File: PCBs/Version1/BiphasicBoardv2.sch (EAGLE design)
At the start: 15 parts

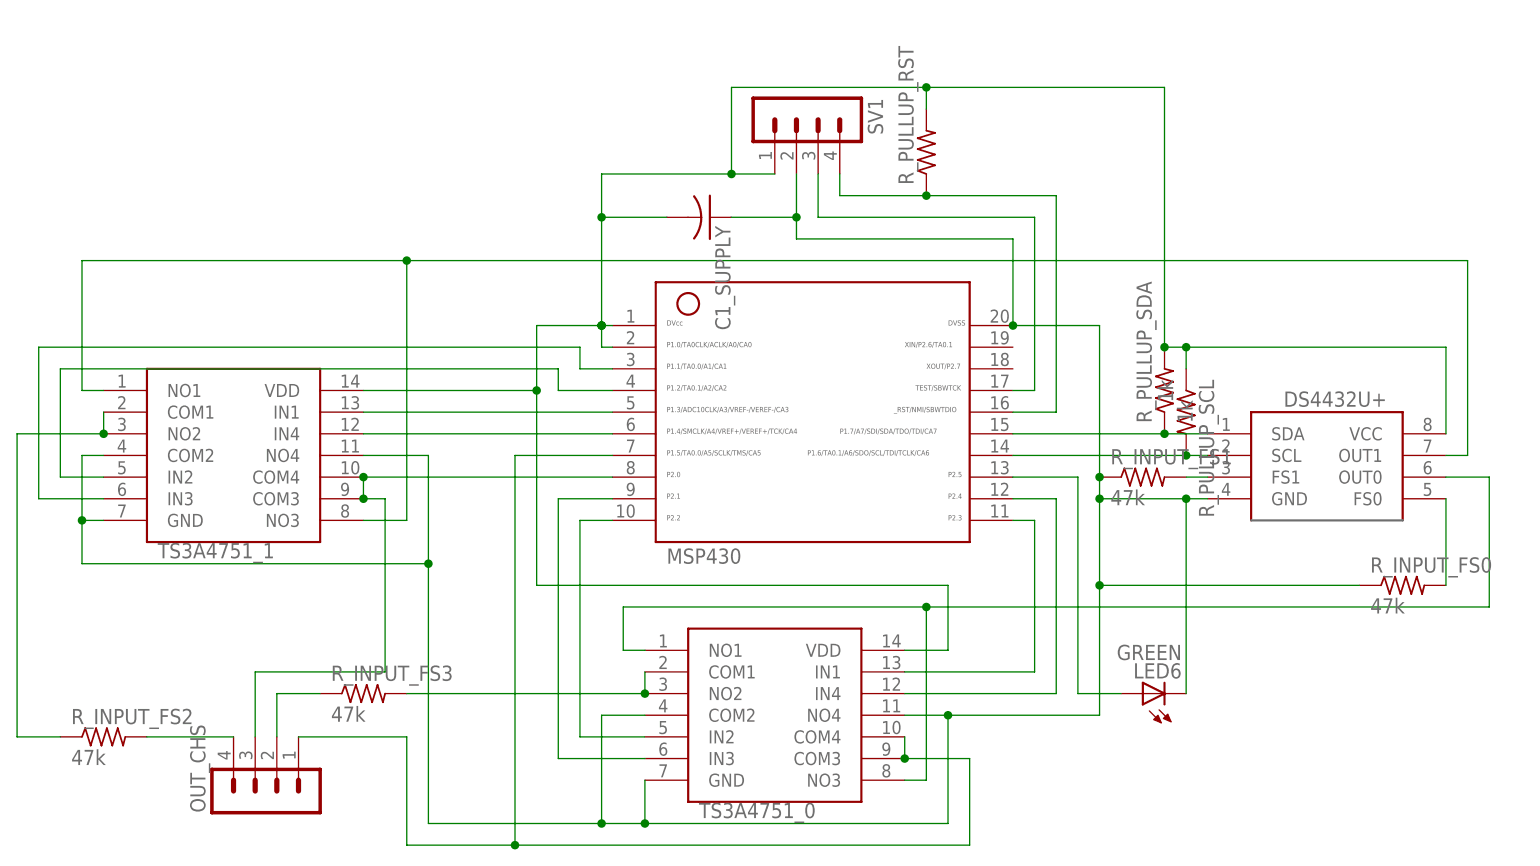
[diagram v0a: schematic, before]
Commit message: Version 1.1 Changes 1) Added a voltage divider to measure power supply level 2) Removed impedence measurement in one of the biphasic current output channels
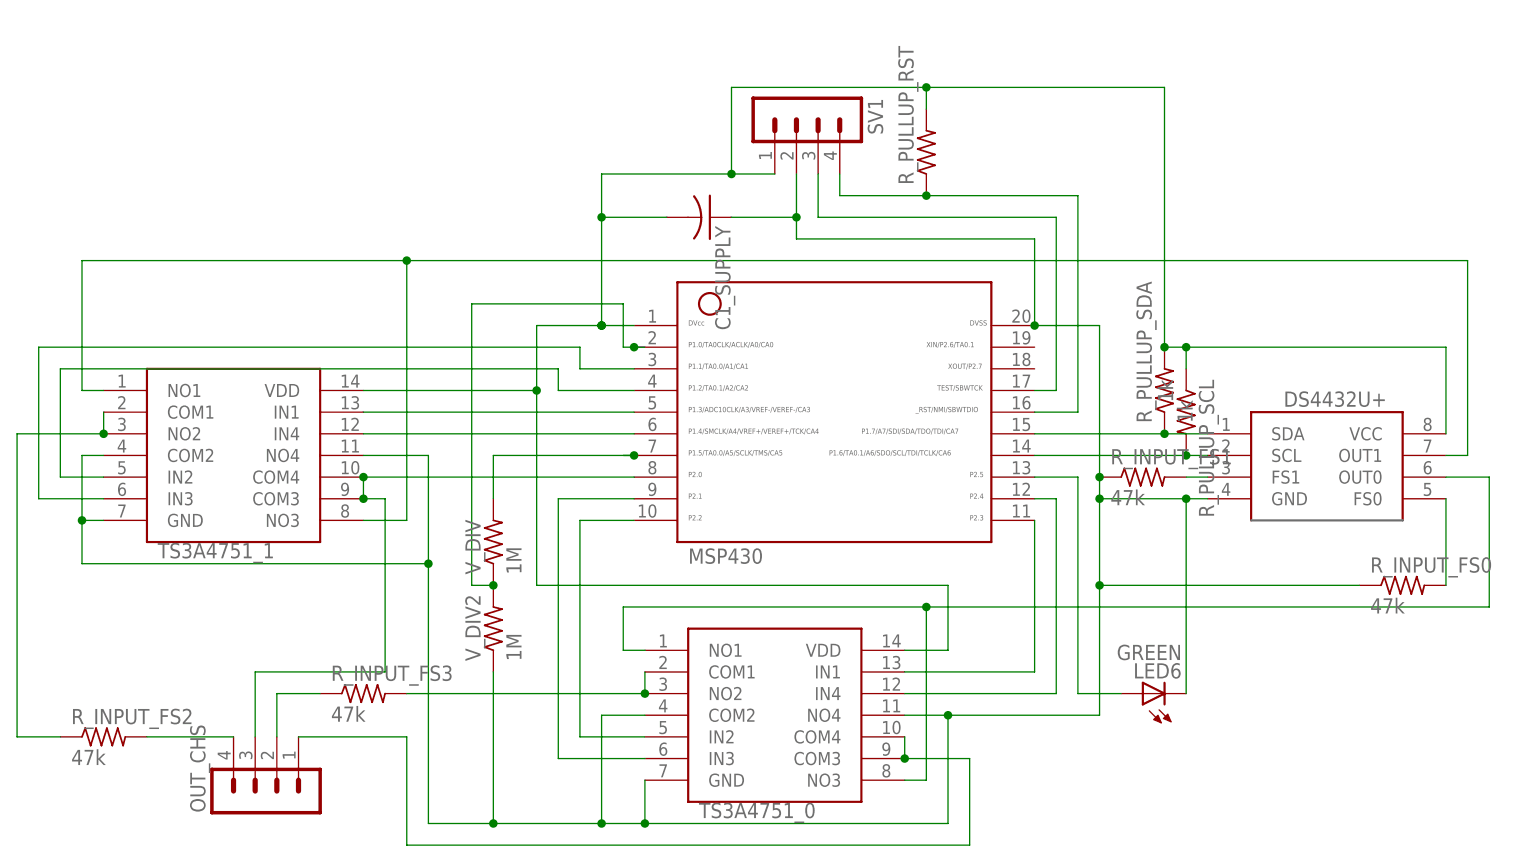
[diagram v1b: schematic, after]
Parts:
- added V_DIV, V_DIV2: 1M, BiphasicBoard:R-US_R0603
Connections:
- new net N$6: MSP430.7, V_DIV.2
- new net N$7: MSP430.2, V_DIV.1, V_DIV2.2
- net GND: now also V_DIV2.1
- net LOAD2_0: no longer MSP430.7
- net VDD: no longer MSP430.2
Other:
- moved on the sheet: MSP430

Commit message: 1) Corrected resistor name&values; 2) Added resistor for LED.
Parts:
- added R_LED: R_LED, BiphasicBoard:R-US_R0603
- R_INPUT_FS1: value 47k -> 43k
- R_LOAD_EX, R_LOAD_EX1: value 47k -> 10k
- R_PULLUP_RST: value (none) -> 43k
- renumbered R_INPUT_FS2 to R_LOAD_EX1, R_INPUT_FS3 to R_LOAD_EX
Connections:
- new net N$9: LED6.C, R_LED.1
- net GND: now also R_LED.2; no longer LED6.C
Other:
- moved on the sheet: R_PULLUP_SCL, R_PULLUP_SDA
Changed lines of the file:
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@@
 <parts>
 <part name="SV1" library="BiphasicBoard" deviceset="MA04-1" device=""/>
-<part name="R_INPUT_FS1" library="BiphasicBoard" deviceset="R-US_" device="R0603" value="47k"/>
+<part name="R_INPUT_FS1" library="BiphasicBoard" deviceset="R-US_" device="R0603" value="43k"/>
 <part name="R_PULLUP_SCL" library="BiphasicBoard" deviceset="R-US_" device="R0603" value="1k"/>
 <part name="R_PULLUP_SDA" library="BiphasicBoard" deviceset="R-US_" device="R0603" value="1k"/>
 <part name="R_INPUT_FS0" library="BiphasicBoard" deviceset="R-US_" device="R0603" value="47k"/>
-<part name="R_PULLUP_RST" library="BiphasicBoard" deviceset="R-US_" device="R0603"/>
+<part name="R_PULLUP_RST" library="BiphasicBoard" deviceset="R-US_" device="R0603" value="43k"/>
 <part name="DS4432U+" library="BiphasicBoard" deviceset="DS4432U+" device=""/>
 <part name="MSP430" library="BiphasicBoard" deviceset="MSP430" device=""/>
@@
 <part name="C1_SUPPLY" library="resistor" deviceset="C-US" device="C0603"/>
 <part name="LED6" library="SparkFun-LED" deviceset="LED" device="1206" value="GREEN"/>
-<part name="R_INPUT_FS2" library="BiphasicBoard" deviceset="R-US_" device="R0603" value="47k"/>
-<part name="R_INPUT_FS3" library="BiphasicBoard" deviceset="R-US_" device="R0603" value="47k"/>
+<part name="R_LOAD_EX1" library="BiphasicBoard" deviceset="R-US_" device="R0603" value="10k"/>
+<part name="R_LOAD_EX" library="BiphasicBoard" deviceset="R-US_" device="R0603" value="10k"/>
 <part name="V_DIV" library="BiphasicBoard" deviceset="R-US_" device="R0603" value="1M"/>
 <part name="V_DIV2" library="BiphasicBoard" deviceset="R-US_" device="R0603" value="1M"/>
+<part name="R_LED" library="BiphasicBoard" deviceset="R-US_" device="R0603" value="R_LED"/>
 </parts>
 <sheets>
@@
 <instance part="SV1" gate="1" x="-20.32" y="106.68" rot="R270"/>
 <instance part="R_INPUT_FS1" gate="G$1" x="17.78" y="63.5"/>
-<instance part="R_PULLUP_SCL" gate="G$1" x="22.86" y="71.12" rot="R270"/>
-<instance part="R_PULLUP_SDA" gate="G$1" x="20.32" y="73.66" rot="R90"/>
+<instance part="R_PULLUP_SCL" gate="G$1" x="22.86" y="76.2" rot="R270"/>
+<instance part="R_PULLUP_SDA" gate="G$1" x="17.78" y="76.2" rot="R90"/>
 <instance part="R_INPUT_FS0" gate="G$1" x="48.26" y="50.8"/>
 <instance part="R_PULLUP_RST" gate="G$1" x="-7.62" y="101.6" rot="R90"/>
@@
 <instance part="C1_SUPPLY" gate="G$1" x="-33.02" y="93.98" rot="R270"/>
 <instance part="LED6" gate="G$1" x="17.78" y="38.1" rot="R90"/>
-<instance part="R_INPUT_FS2" gate="G$1" x="-104.14" y="33.02"/>
-<instance part="R_INPUT_FS3" gate="G$1" x="-73.66" y="38.1"/>
+<instance part="R_LOAD_EX1" gate="G$1" x="-104.14" y="33.02"/>
+<instance part="R_LOAD_EX" gate="G$1" x="-73.66" y="38.1"/>
 <instance part="V_DIV" gate="G$1" x="-58.42" y="55.88" rot="R90"/>
 <instance part="V_DIV2" gate="G$1" x="-58.42" y="45.72" rot="R90"/>
+<instance part="R_LED" gate="G$1" x="22.86" y="48.26" rot="R90"/>
 </instances>
 <busses>
@@
 <wire x1="5.08" y1="66.04" x2="22.86" y2="66.04" width="0.1524" layer="91"/>
 <pinref part="R_PULLUP_SCL" gate="G$1" pin="2"/>
+<wire x1="22.86" y1="71.12" x2="22.86" y2="66.04" width="0.1524" layer="91"/>
 <wire x1="22.86" y1="66.04" x2="25.4" y2="66.04" width="0.1524" layer="91"/>
-<junction x="22.86" y="66.04"/>
 <pinref part="DS4432U+" gate="G$1" pin="SCL"/>
 <pinref part="MSP430" gate="G$1" pin="14"/>
+<junction x="22.86" y="66.04"/>
 </segment>
 </net>
 <net name="N$2" class="0">
 <segment>
-<wire x1="5.08" y1="68.58" x2="20.32" y2="68.58" width="0.1524" layer="91"/>
+<wire x1="5.08" y1="68.58" x2="17.78" y2="68.58" width="0.1524" layer="91"/>
 <pinref part="R_PULLUP_SDA" gate="G$1" pin="1"/>
-<wire x1="20.32" y1="68.58" x2="25.4" y2="68.58" width="0.1524" layer="91"/>
-<junction x="20.32" y="68.58"/>
+<wire x1="17.78" y1="71.12" x2="17.78" y2="68.58" width="0.1524" layer="91"/>
+<wire x1="17.78" y1="68.58" x2="25.4" y2="68.58" width="0.1524" layer="91"/>
 <pinref part="DS4432U+" gate="G$1" pin="SDA"/>
 <pinref part="MSP430" gate="G$1" pin="15"/>
+<junction x="17.78" y="68.58"/>
 </segment>
 </net>
@@
 <wire x1="-30.48" y1="109.22" x2="-7.62" y2="109.22" width="0.1524" layer="91"/>
 <pinref part="R_PULLUP_SDA" gate="G$1" pin="2"/>
-<wire x1="-7.62" y1="109.22" x2="20.32" y2="109.22" width="0.1524" layer="91"/>
-<wire x1="20.32" y1="109.22" x2="20.32" y2="78.74" width="0.1524" layer="91"/>
-<wire x1="20.32" y1="78.74" x2="22.86" y2="78.74" width="0.1524" layer="91"/>
-<wire x1="22.86" y1="78.74" x2="53.34" y2="78.74" width="0.1524" layer="91"/>
-<wire x1="53.34" y1="78.74" x2="53.34" y2="68.58" width="0.1524" layer="91"/>
+<wire x1="-7.62" y1="109.22" x2="17.78" y2="109.22" width="0.1524" layer="91"/>
+<wire x1="17.78" y1="109.22" x2="17.78" y2="83.82" width="0.1524" layer="91"/>
+<wire x1="17.78" y1="81.28" x2="17.78" y2="83.82" width="0.1524" layer="91"/>
+<wire x1="17.78" y1="83.82" x2="22.86" y2="83.82" width="0.1524" layer="91"/>
+<wire x1="22.86" y1="81.28" x2="22.86" y2="83.82" width="0.1524" layer="91"/>
+<wire x1="22.86" y1="83.82" x2="53.34" y2="83.82" width="0.1524" layer="91"/>
+<wire x1="53.34" y1="83.82" x2="53.34" y2="68.58" width="0.1524" layer="91"/>
 <pinref part="R_PULLUP_SCL" gate="G$1" pin="1"/>
-<wire x1="22.86" y1="78.74" x2="22.86" y2="76.2" width="0.1524" layer="91"/>
-<junction x="22.86" y="78.74"/>
-<junction x="20.32" y="78.74"/>
 <junction x="-30.48" y="99.06"/>
 <junction x="-45.72" y="81.28"/>
@@
 <junction x="-45.72" y="93.98"/>
 <junction x="-45.72" y="81.28"/>
+<junction x="17.78" y="83.82"/>
+<junction x="22.86" y="83.82"/>
 </segment>
 </net>
@@
 <wire x1="-30.48" y1="93.98" x2="-22.86" y2="93.98" width="0.1524" layer="91"/>
 <junction x="-22.86" y="93.98"/>
-<pinref part="LED6" gate="G$1" pin="C"/>
-<wire x1="22.86" y1="38.1" x2="22.86" y2="60.96" width="0.1524" layer="91"/>
 <junction x="22.86" y="60.96"/>
 <junction x="-58.42" y="22.86"/>
 <pinref part="V_DIV2" gate="G$1" pin="1"/>
+<wire x1="22.86" y1="53.34" x2="22.86" y2="60.96" width="0.1524" layer="91"/>
 <wire x1="-58.42" y1="40.64" x2="-58.42" y2="22.86" width="0.1524" layer="91"/>
+<pinref part="R_LED" gate="G$1" pin="2"/>
 </segment>
 </net>
@@
 <pinref part="TS3A4751_0" gate="G$1" pin="COM1"/>
 <junction x="-40.64" y="38.1"/>
-<pinref part="R_INPUT_FS3" gate="G$1" pin="2"/>
+<pinref part="R_LOAD_EX" gate="G$1" pin="2"/>
 <wire x1="-68.58" y1="38.1" x2="-40.64" y2="38.1" width="0.1524" layer="91"/>
 </segment>
@@
 <wire x1="-114.3" y1="33.02" x2="-109.22" y2="33.02" width="0.1524" layer="91"/>
 <junction x="-104.14" y="68.58"/>
-<pinref part="R_INPUT_FS2" gate="G$1" pin="1"/>
+<pinref part="R_LOAD_EX1" gate="G$1" pin="1"/>
 </segment>
 </net>
@@
 <segment>
 <pinref part="OUT_CHS" gate="1" pin="4"/>
-<pinref part="R_INPUT_FS2" gate="G$1" pin="2"/>
+<pinref part="R_LOAD_EX1" gate="G$1" pin="2"/>
 <wire x1="-99.06" y1="33.02" x2="-88.9" y2="33.02" width="0.1524" layer="91"/>
 </segment>
@@
 <wire x1="-83.82" y1="33.02" x2="-83.82" y2="38.1" width="0.1524" layer="91"/>
 <wire x1="-83.82" y1="38.1" x2="-78.74" y2="38.1" width="0.1524" layer="91"/>
-<pinref part="R_INPUT_FS3" gate="G$1" pin="1"/>
+<pinref part="R_LOAD_EX" gate="G$1" pin="1"/>
 </segment>
 </net>
@@
 </segment>
 </net>
+<net name="N$9" class="0">
+<segment>
+<pinref part="R_LED" gate="G$1" pin="1"/>
+<pinref part="LED6" gate="G$1" pin="C"/>
+<wire x1="22.86" y1="38.1" x2="22.86" y2="43.18" width="0.1524" layer="91"/>
+</segment>
+</net>
